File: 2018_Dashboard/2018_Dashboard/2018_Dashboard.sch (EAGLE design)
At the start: 51 parts, among them Y1 16MHz

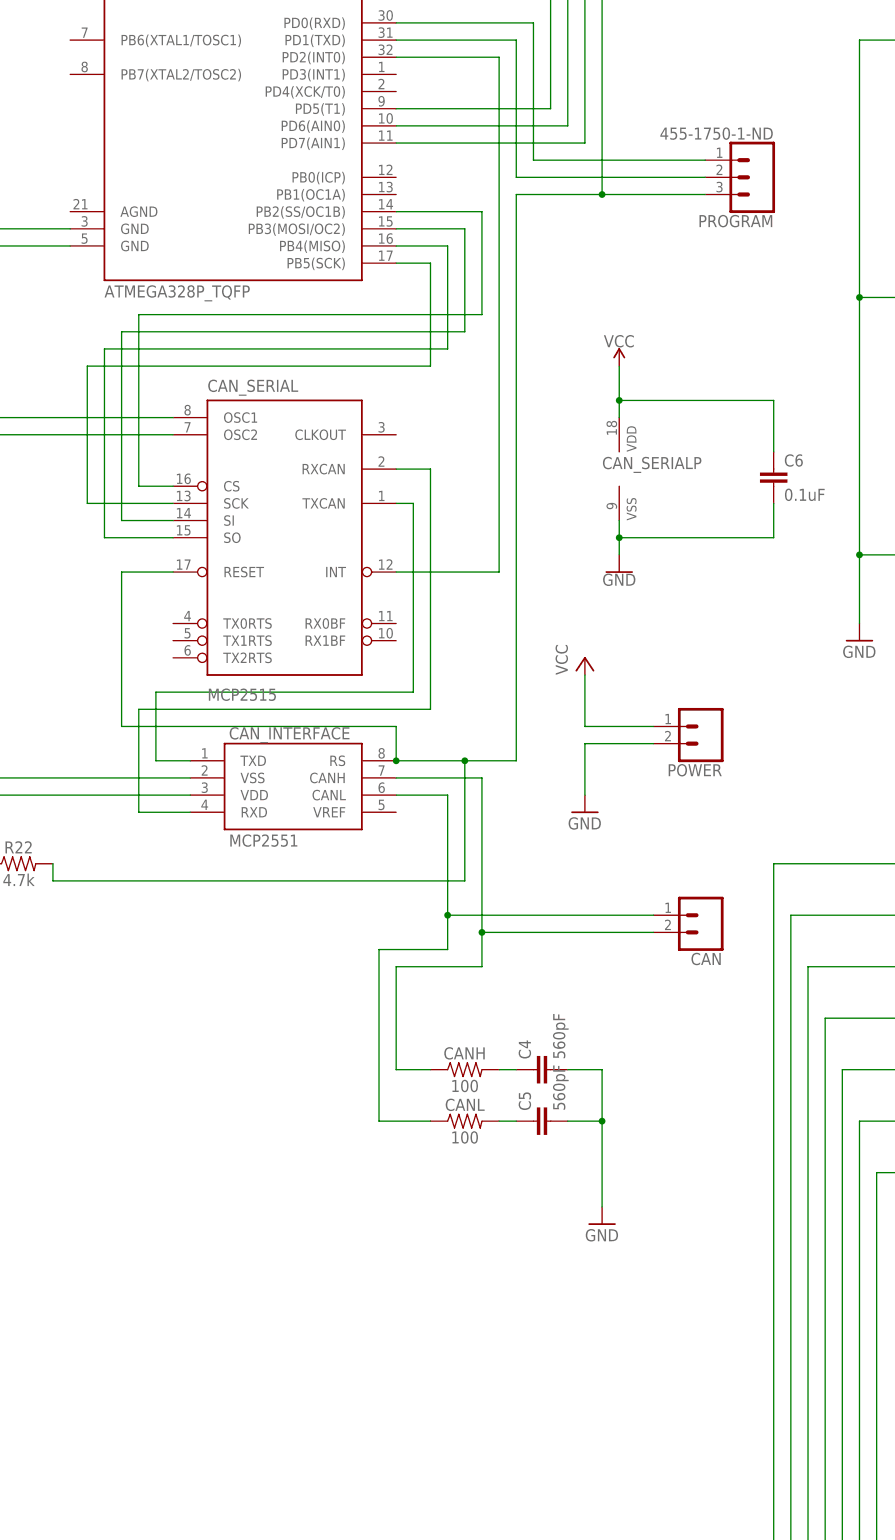
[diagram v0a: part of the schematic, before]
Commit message: Post order changes for 2019 car: Made board more narrow Added breakout headers for buring bootloader git commit -m
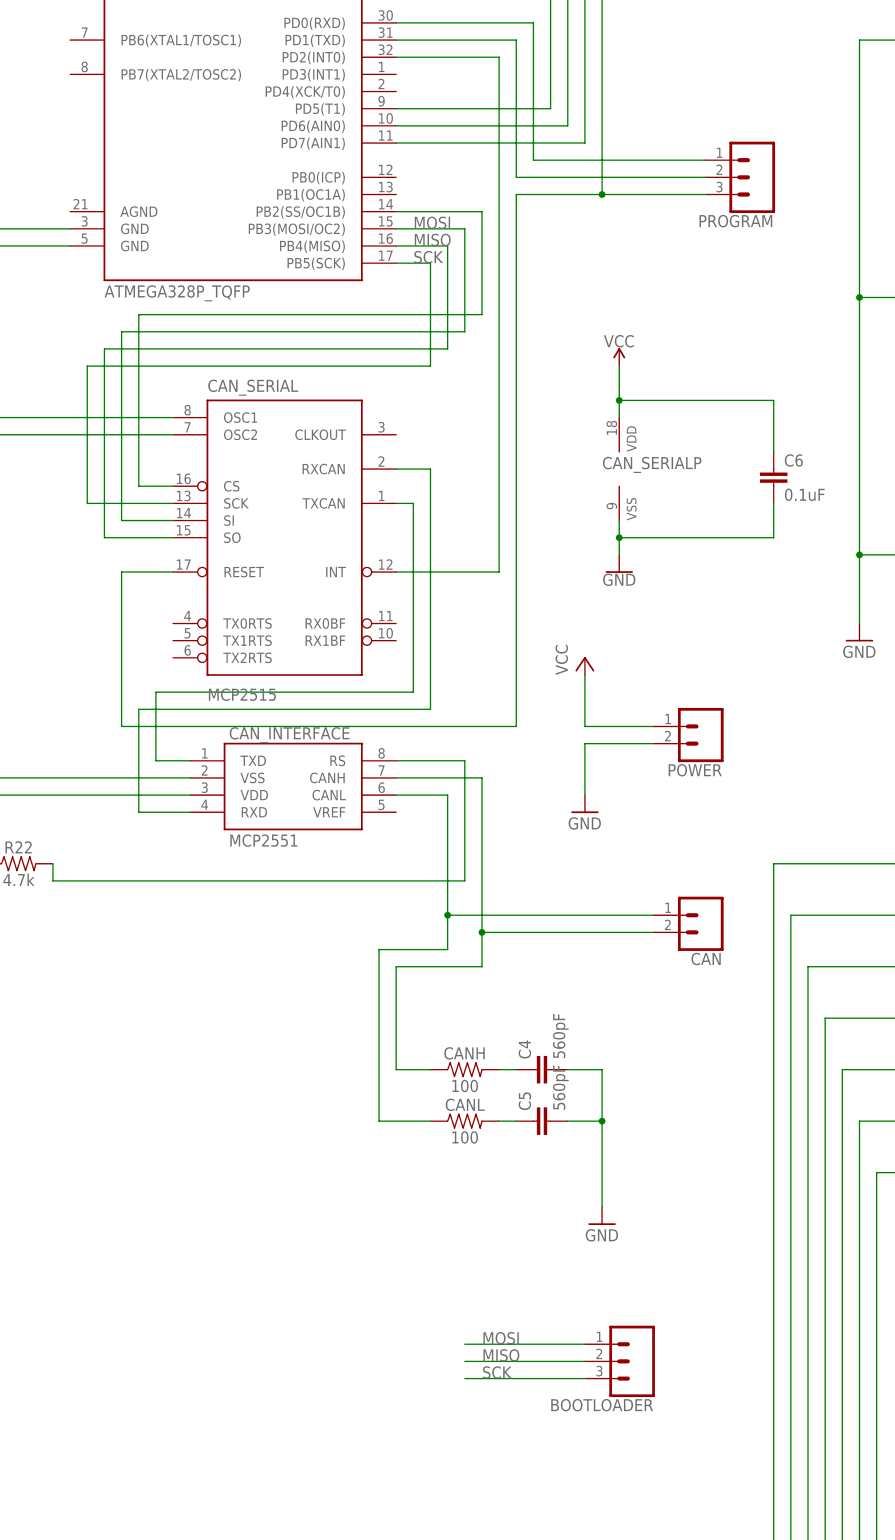
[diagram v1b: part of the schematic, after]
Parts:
- added BOOTLOADER: (no value), SparkFun-Connectors:CONN_03
- PROGRAM: value 455-1750-1-ND -> (none)
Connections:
- net N$67 renamed RX
- net N$68 renamed TX
- removed net N$53: CAN_SERIAL>NAME.SI, CONTROL.PB3(MOSI/OC2)
- removed net N$54: CAN_SERIAL>NAME.SO, CONTROL.PB4(MISO)
- removed net N$55: CAN_SERIAL>NAME.SCK, CONTROL.PB5(SCK)
- removed net N$61: CAN_INTERFACE.RS, CAN_SERIAL>NAME.RESET, CONTROL.PC6(/RESET), PROGRAM.3, R21.2, R22.2
- new net MISO: BOOTLOADER.2, CAN_SERIAL>NAME.SO, CONTROL.PB4(MISO)
- new net MOSI: BOOTLOADER.1, CAN_SERIAL>NAME.SI, CONTROL.PB3(MOSI/OC2)
- new net N$1: CAN_INTERFACE.RS, R22.2
- new net RST: CAN_SERIAL>NAME.RESET, CONTROL.PC6(/RESET), PROGRAM.3, R21.2
- new net SCK: BOOTLOADER.3, CAN_SERIAL>NAME.SCK, CONTROL.PB5(SCK)
